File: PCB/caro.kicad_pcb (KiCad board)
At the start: 2 copper layers, 83.8 x 33 mm, 10 parts, among them SW1 Power Switch, SW2 Control Button, U1 DFR0299

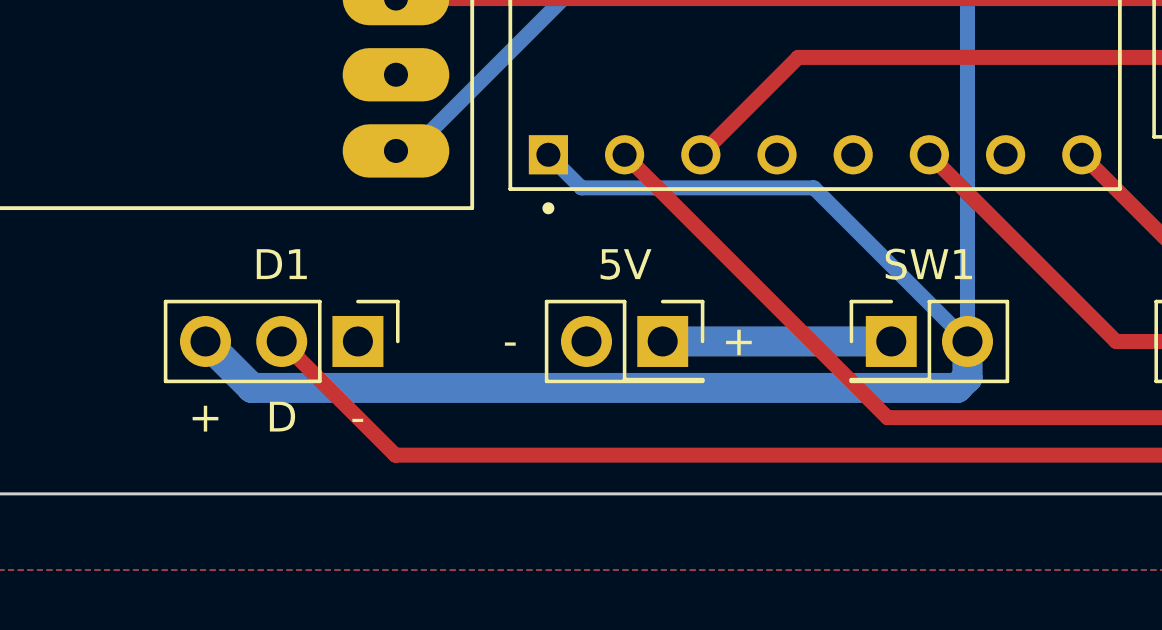
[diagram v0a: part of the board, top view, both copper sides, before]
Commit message: Corrected inverted LED pins
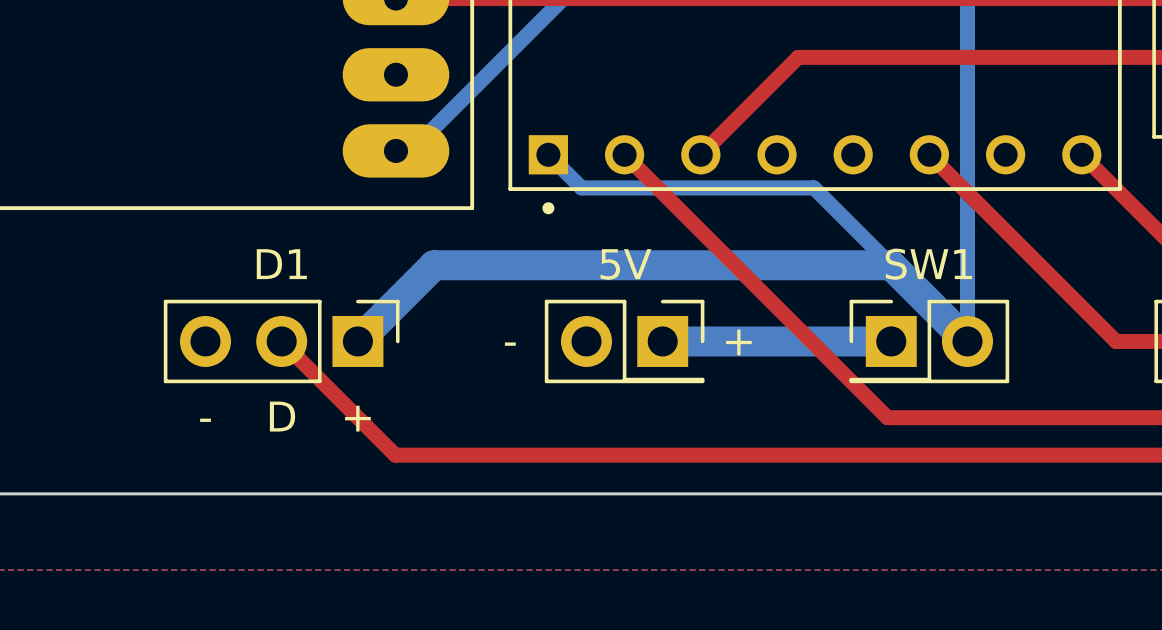
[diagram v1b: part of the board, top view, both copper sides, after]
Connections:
- D1 pad 1: GND -> 5V
- D1 pad 2: Net-(D1-Pad4) -> unconnected-(D1-Pad2)
- D1 pad 3: 5V -> GND
- R1 pad 1: Net-(D1-Pad4) -> D6
- R1 pad 2: D6 -> Net-(D1-Pad4)
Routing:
- net unconnected-(D1-Pad2): track 0.00 -> 60.0 mm
- net Net-(D1-Pad4): track 60.0 -> 20.1 mm
- net D6: track 20.1 -> 0.00 mm
- net 5V: track 71.6 -> 63.0 mm
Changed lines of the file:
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@@
   (net 46 "unconnected-(U1-Pad9)")
   (net 47 "+5V")
+  (net 48 "unconnected-(D1-Pad2)")
   (footprint "Module:Arduino_Nano" placed (layer "F.Cu")
     (at 147.32 101 90)
@@
     (fp_line (start -1.27 -0.635) (end -0.635 -1.27) (layer "F.Fab") (width 0.1))
     (pad "1" thru_hole rect locked (at 0 0 270) (size 1.7 1.7) (drill 1) (layers *.Cu *.Mask)
-      (net 7 "GND") (pinfunction "VDD") (pintype "power_in"))
+      (net 27 "5V") (pinfunction "VDD") (pintype "power_in"))
     (pad "2" thru_hole oval locked (at 0 2.54 270) (size 1.7 1.7) (drill 1) (layers *.Cu *.Mask)
-      (net 30 "Net-(D1-Pad4)") (pinfunction "DOUT") (pintype "output"))
+      (net 48 "unconnected-(D1-Pad2)") (pinfunction "DOUT") (pintype "output"))
     (pad "3" thru_hole oval locked (at 0 5.08 270) (size 1.7 1.7) (drill 1) (layers *.Cu *.Mask)
-      (net 27 "5V") (pinfunction "VSS") (pintype "power_in"))
+      (net 7 "GND") (pinfunction "VSS") (pintype "power_in"))
     (model "${KISYS3DMOD}/Connector_PinHeader_2.54mm.3dshapes/PinHeader_1x03_P2.54mm_Vertical.wrl"
       (offset (xyz 0 0 0))
@@
     (fp_line (start 14.66 1.6) (end 14.66 -1.6) (layer "F.Fab") (width 0.1))
     (pad "1" thru_hole circle locked (at 0 0) (size 1.6 1.6) (drill 0.8) (layers *.Cu *.Mask)
+      (net 17 "D6") (pintype "passive"))
+    (pad "2" thru_hole oval locked (at 20.32 0) (size 1.6 1.6) (drill 0.8) (layers *.Cu *.Mask)
       (net 30 "Net-(D1-Pad4)") (pintype "passive"))
-    (pad "2" thru_hole oval locked (at 20.32 0) (size 1.6 1.6) (drill 0.8) (layers *.Cu *.Mask)
-      (net 17 "D6") (pintype "passive"))
     (model "${KISYS3DMOD}/Resistor_THT.3dshapes/R_Axial_DIN0309_L9.0mm_D3.2mm_P20.32mm_Horizontal.wrl"
       (offset (xyz 0 0 0))
@@
     (effects (font (size 1 1) (thickness 0.15)))
   )
-  (gr_text "+" (at 111.76 111.76) (layer "F.SilkS")
+  (gr_text "+" (at 116.84 111.76) (layer "F.SilkS")
     (effects (font (size 1 1) (thickness 0.15)))
   )
@@
     (effects (font (size 1 1) (thickness 0.15)))
   )
-  (gr_text "-" (at 116.84 111.76) (layer "F.SilkS")
+  (gr_text "-" (at 111.76 111.76) (layer "F.SilkS")
     (effects (font (size 1 1) (thickness 0.15)))
   )
@@
   (segment (start 118.11 97.79) (end 150.53 97.79) (width 0.5) (layer "F.Cu") (net 16))
   (segment (start 150.53 97.79) (end 162.56 85.76) (width 0.5) (layer "F.Cu") (net 16))
-  (segment (start 173.32 106.68) (end 185.42 106.68) (width 0.5) (layer "F.Cu") (net 17))
-  (segment (start 167.64 101) (end 173.32 106.68) (width 0.5) (layer "F.Cu") (net 17))
   (segment (start 128.27 102.997) (end 131.516511 99.750489) (width 0.5) (layer "F.Cu") (net 19))
   (segment (start 131.516511 99.750489) (end 168.930489 99.750489) (width 0.5) (layer "F.Cu") (net 19))
   (segment (start 168.930489 99.750489) (end 170.18 101) (width 0.5) (layer "F.Cu") (net 19))
+  (segment (start 132.040511 104.100511) (end 134.62 106.68) (width 0.5) (layer "B.Cu") (net 27))
   (segment (start 124.293511 104.100511) (end 132.040511 104.100511) (width 0.5) (layer "B.Cu") (net 27))
-  (segment (start 136.81257 110.769511) (end 137.16 110.422081) (width 1) (layer "B.Cu") (net 27))
+  (segment (start 119.38 106.68) (end 134.62 106.68) (width 1) (layer "B.Cu") (net 27))
   (segment (start 123.19 102.997) (end 124.293511 104.100511) (width 0.5) (layer "B.Cu") (net 27))
-  (segment (start 132.040511 104.100511) (end 137.16 109.22) (width 0.5) (layer "B.Cu") (net 27))
-  (segment (start 111.76 109.22) (end 113.309511 110.769511) (width 1) (layer "B.Cu") (net 27))
   (segment (start 137.16 95.92) (end 147.32 85.76) (width 0.5) (layer "B.Cu") (net 27))
-  (segment (start 113.309511 110.769511) (end 136.81257 110.769511) (width 1) (layer "B.Cu") (net 27))
-  (segment (start 137.16 110.422081) (end 137.16 109.22) (width 1) (layer "B.Cu") (net 27))
+  (segment (start 116.84 109.22) (end 119.38 106.68) (width 1) (layer "B.Cu") (net 27))
+  (segment (start 134.62 106.68) (end 137.16 109.22) (width 1) (layer "B.Cu") (net 27))
   (segment (start 137.16 109.22) (end 137.16 95.92) (width 0.5) (layer "B.Cu") (net 27))
-  (segment (start 118.089511 113.009511) (end 165.617565 113.009511) (width 0.5) (layer "F.Cu") (net 30))
-  (segment (start 114.3 109.22) (end 118.089511 113.009511) (width 0.5) (layer "F.Cu") (net 30))
-  (segment (start 165.617565 113.009511) (end 166.349511 112.277565) (width 0.5) (layer "F.Cu") (net 30))
-  (segment (start 166.349511 112.277565) (end 166.349511 107.929511) (width 0.5) (layer "F.Cu") (net 30))
-  (segment (start 166.349511 107.929511) (end 165.1 106.68) (width 0.5) (layer "F.Cu") (net 30))
+  (segment (start 173.32 106.68) (end 185.42 106.68) (width 0.5) (layer "F.Cu") (net 30))
+  (segment (start 167.64 101) (end 173.32 106.68) (width 0.5) (layer "F.Cu") (net 30))
   (segment (start 134.493 111.76) (end 165.1 111.76) (width 0.5) (layer "F.Cu") (net 31))
   (segment (start 125.73 102.997) (end 134.493 111.76) (width 0.5) (layer "F.Cu") (net 31))
@@
   (segment (start 147.193 109.22) (end 147.32 109.22) (width 0.5) (layer "F.Cu") (net 45))
   (segment (start 127 109.22) (end 134.62 109.22) (width 1) (layer "B.Cu") (net 47))
+  (segment (start 118.089511 113.009511) (end 165.617565 113.009511) (width 0.5) (layer "F.Cu") (net 48))
+  (segment (start 114.3 109.22) (end 118.089511 113.009511) (width 0.5) (layer "F.Cu") (net 48))
+  (segment (start 165.617565 113.009511) (end 166.349511 112.277565) (width 0.5) (layer "F.Cu") (net 48))
+  (segment (start 166.349511 112.277565) (end 166.349511 107.929511) (width 0.5) (layer "F.Cu") (net 48))
+  (segment (start 166.349511 107.929511) (end 165.1 106.68) (width 0.5) (layer "F.Cu") (net 48))
   (zone (net 7) (net_name "GND") (layers F&B.Cu) (name "gnd") (hatch edge 0.508)
     (connect_pads (clearance 0.508))

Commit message: Bump to v1.1
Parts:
- moved R1 20.3 mm to (185.4, 106.7), turned to 180 degrees
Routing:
- net Net-(D1-Pad4): track 20.1 -> 0.00 mm
- net D6: track 0.00 -> 20.1 mm
- net 5V: track 63.0 -> 66.3 mm
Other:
- board text added: "Lightsaber v1.1 PCB Design by @simonmicro"
- board text removed: "Lightsaber v1.0 PCB Design by @simonmicro"
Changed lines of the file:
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@@
   )
   (footprint "Resistor_THT:R_Axial_DIN0309_L9.0mm_D3.2mm_P20.32mm_Horizontal" placed (layer "F.Cu")
-    (at 165.1 106.68)
+    (at 185.42 106.68 180)
     (descr "Resistor, Axial_DIN0309 series, Axial, Horizontal, pin pitch=20.32mm, 0.5W = 1/2W, length*diameter=9*3.2mm^2, http://cdn-reichelt.de/documents/datenblatt/B400/1_4W%23YAG.pdf")
     (tags "Resistor Axial_DIN0309 series Axial Horizontal pin pitch 20.32mm 0.5W = 1/2W length 9mm diameter 3.2mm")
@@
     (fp_line (start 5.66 -1.6) (end 5.66 1.6) (layer "F.Fab") (width 0.1))
     (fp_line (start 14.66 1.6) (end 14.66 -1.6) (layer "F.Fab") (width 0.1))
-    (pad "1" thru_hole circle locked (at 0 0) (size 1.6 1.6) (drill 0.8) (layers *.Cu *.Mask)
+    (pad "1" thru_hole circle locked (at 0 0 180) (size 1.6 1.6) (drill 0.8) (layers *.Cu *.Mask)
       (net 17 "D6") (pintype "passive"))
-    (pad "2" thru_hole oval locked (at 20.32 0) (size 1.6 1.6) (drill 0.8) (layers *.Cu *.Mask)
+    (pad "2" thru_hole oval locked (at 20.32 0 180) (size 1.6 1.6) (drill 0.8) (layers *.Cu *.Mask)
       (net 30 "Net-(D1-Pad4)") (pintype "passive"))
     (model "${KISYS3DMOD}/Resistor_THT.3dshapes/R_Axial_DIN0309_L9.0mm_D3.2mm_P20.32mm_Horizontal.wrl"
@@
     (effects (font (size 1 1) (thickness 0.15)))
   )
-  (gr_text "Lightsaber v1.0\nPCB Design by @simonmicro" (at 165.1 93.98) (layer "F.SilkS")
+  (gr_text "Lightsaber v1.1\nPCB Design by @simonmicro" (at 165.1 93.98) (layer "F.SilkS")
     (effects (font (size 1 1) (thickness 0.15)))
   )
@@
   (segment (start 118.11 97.79) (end 150.53 97.79) (width 0.5) (layer "F.Cu") (net 16))
   (segment (start 150.53 97.79) (end 162.56 85.76) (width 0.5) (layer "F.Cu") (net 16))
+  (segment (start 185.42 106.68) (end 173.32 106.68) (width 0.5) (layer "F.Cu") (net 17))
+  (segment (start 173.32 106.68) (end 167.64 101) (width 0.5) (layer "F.Cu") (net 17))
   (segment (start 128.27 102.997) (end 131.516511 99.750489) (width 0.5) (layer "F.Cu") (net 19))
   (segment (start 131.516511 99.750489) (end 168.930489 99.750489) (width 0.5) (layer "F.Cu") (net 19))
   (segment (start 168.930489 99.750489) (end 170.18 101) (width 0.5) (layer "F.Cu") (net 19))
-  (segment (start 132.040511 104.100511) (end 134.62 106.68) (width 0.5) (layer "B.Cu") (net 27))
   (segment (start 124.293511 104.100511) (end 132.040511 104.100511) (width 0.5) (layer "B.Cu") (net 27))
-  (segment (start 119.38 106.68) (end 134.62 106.68) (width 1) (layer "B.Cu") (net 27))
   (segment (start 123.19 102.997) (end 124.293511 104.100511) (width 0.5) (layer "B.Cu") (net 27))
+  (segment (start 137.16 106.68) (end 134.580511 104.100511) (width 0.5) (layer "B.Cu") (net 27))
+  (segment (start 137.16 109.22) (end 137.16 106.68) (width 0.5) (layer "B.Cu") (net 27))
   (segment (start 137.16 95.92) (end 147.32 85.76) (width 0.5) (layer "B.Cu") (net 27))
-  (segment (start 116.84 109.22) (end 119.38 106.68) (width 1) (layer "B.Cu") (net 27))
-  (segment (start 134.62 106.68) (end 137.16 109.22) (width 1) (layer "B.Cu") (net 27))
-  (segment (start 137.16 109.22) (end 137.16 95.92) (width 0.5) (layer "B.Cu") (net 27))
-  (segment (start 173.32 106.68) (end 185.42 106.68) (width 0.5) (layer "F.Cu") (net 30))
-  (segment (start 167.64 101) (end 173.32 106.68) (width 0.5) (layer "F.Cu") (net 30))
+  (segment (start 135.822081 111.76) (end 137.16 110.422081) (width 1) (layer "B.Cu") (net 27))
+  (segment (start 134.580511 104.100511) (end 132.040511 104.100511) (width 0.5) (layer "B.Cu") (net 27))
+  (segment (start 137.16 110.422081) (end 137.16 109.22) (width 1) (layer "B.Cu") (net 27))
+  (segment (start 137.16 106.68) (end 137.16 95.92) (width 0.5) (layer "B.Cu") (net 27))
+  (segment (start 119.38 111.76) (end 135.822081 111.76) (width 1) (layer "B.Cu") (net 27))
+  (segment (start 116.84 109.22) (end 119.38 111.76) (width 1) (layer "B.Cu") (net 27))
   (segment (start 134.493 111.76) (end 165.1 111.76) (width 0.5) (layer "F.Cu") (net 31))
   (segment (start 125.73 102.997) (end 134.493 111.76) (width 0.5) (layer "F.Cu") (net 31))
@@
   (segment (start 147.193 109.22) (end 147.32 109.22) (width 0.5) (layer "F.Cu") (net 45))
   (segment (start 127 109.22) (end 134.62 109.22) (width 1) (layer "B.Cu") (net 47))
-  (segment (start 118.089511 113.009511) (end 165.617565 113.009511) (width 0.5) (layer "F.Cu") (net 48))
-  (segment (start 114.3 109.22) (end 118.089511 113.009511) (width 0.5) (layer "F.Cu") (net 48))
+  (segment (start 164.216462 112.643538) (end 164.582435 113.009511) (width 0.5) (layer "F.Cu") (net 48))
+  (segment (start 166.349511 112.277565) (end 166.349511 107.929511) (width 0.5) (layer "F.Cu") (net 48))
   (segment (start 165.617565 113.009511) (end 166.349511 112.277565) (width 0.5) (layer "F.Cu") (net 48))
-  (segment (start 166.349511 112.277565) (end 166.349511 107.929511) (width 0.5) (layer "F.Cu") (net 48))
   (segment (start 166.349511 107.929511) (end 165.1 106.68) (width 0.5) (layer "F.Cu") (net 48))
+  (segment (start 117.723538 112.643538) (end 164.216462 112.643538) (width 0.5) (layer "F.Cu") (net 48))
+  (segment (start 114.3 109.22) (end 117.723538 112.643538) (width 0.5) (layer "F.Cu") (net 48))
+  (segment (start 164.582435 113.009511) (end 165.617565 113.009511) (width 0.5) (layer "F.Cu") (net 48))
   (zone (net 7) (net_name "GND") (layers F&B.Cu) (name "gnd") (hatch edge 0.508)
     (connect_pads (clearance 0.508))

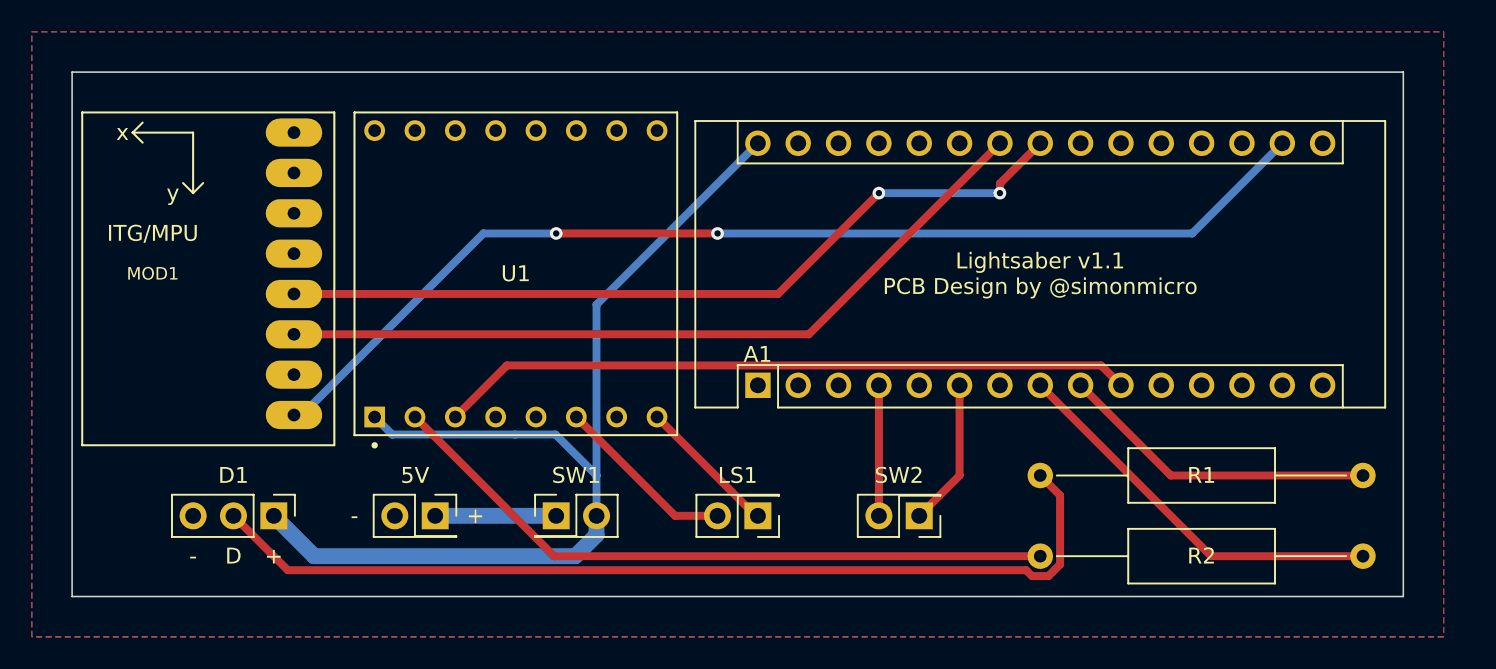
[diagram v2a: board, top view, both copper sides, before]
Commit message: Updated annotations Added missing control LED Reduced resistor sizes
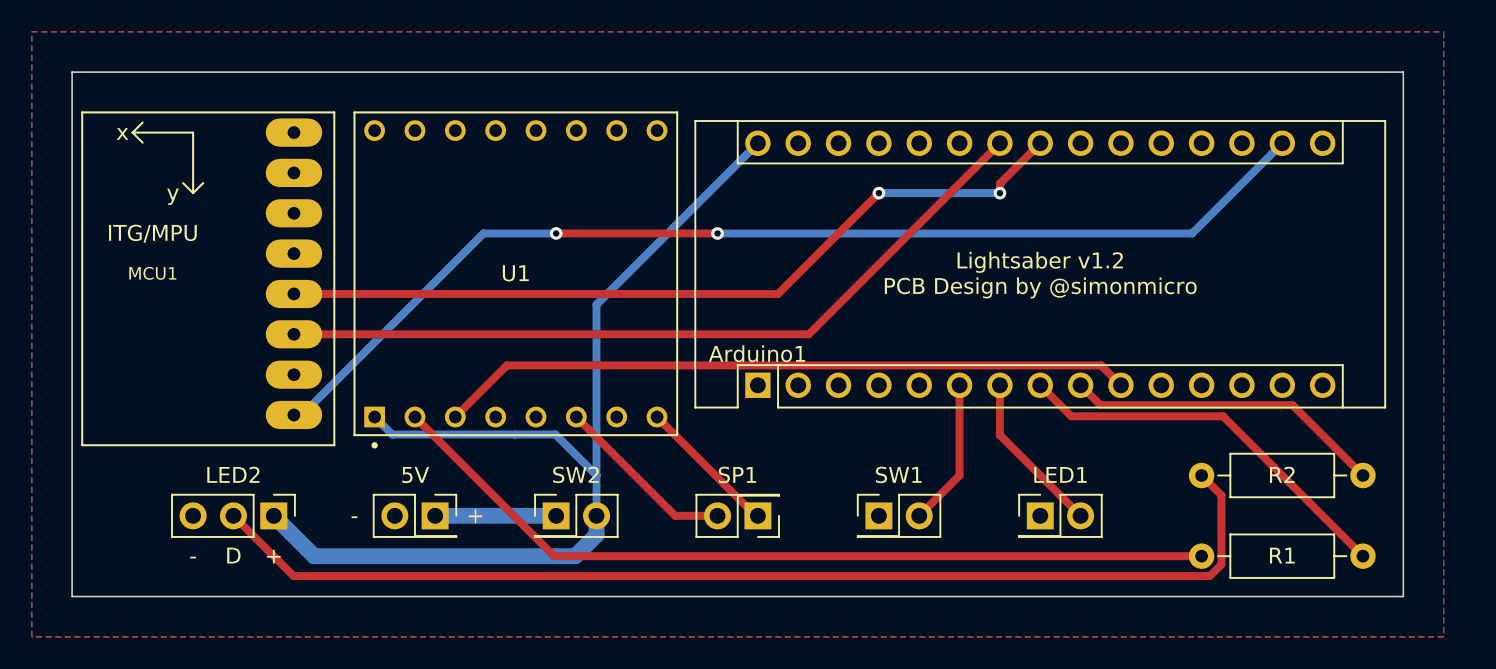
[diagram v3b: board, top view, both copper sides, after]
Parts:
- added LED1: Control Button LED, Connector_PinHeader_2.54mm:PinHeader_2x01_P2.54mm_Vertical, F.Cu at (165.1, 109.2)
- R1: renamed from R2; footprint Resistor_THT:R_Axial_DIN0309_L9.0mm_D3.2mm_P20.32mm_Horizontal -> Resistor_THT:R_Axial_DIN0207_L6.3mm_D2.5mm_P10.16mm_Horizontal
- R2: renamed from R1; footprint Resistor_THT:R_Axial_DIN0309_L9.0mm_D3.2mm_P20.32mm_Horizontal -> Resistor_THT:R_Axial_DIN0207_L6.3mm_D2.5mm_P10.16mm_Horizontal
- moved SW1 2.54 mm to (154.9, 109.2), turned to 0 degrees
- renumbered A1 to Arduino1, D1 to LED2, MOD1 to MCU1, LS1 to SP1, SW2 to SW1, SW1 to SW2
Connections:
- Arduino1 pad 7: unconnected-(A1-Pad7) -> D4
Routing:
- net Net-(LED2-Pad4): track 0.00 -> 70.2 mm
- net unconnected-(LED2-Pad2): track 60.0 -> 0.00 mm
- net D4: track 0.00 -> 10.3 mm
- net Net-(U1-Pad2): track 43.0 -> 53.2 mm
- net D3: track 9.27 -> 0.00 mm
- net GND: track 8.22 -> 9.27 mm
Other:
- board text added: "Lightsaber v1.2 PCB Design by @simonmicro"
- board text removed: "Lightsaber v1.1 PCB Design by @simonmicro"

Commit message: Revision v1.3 Increased HIGH_PWR width to 2mm
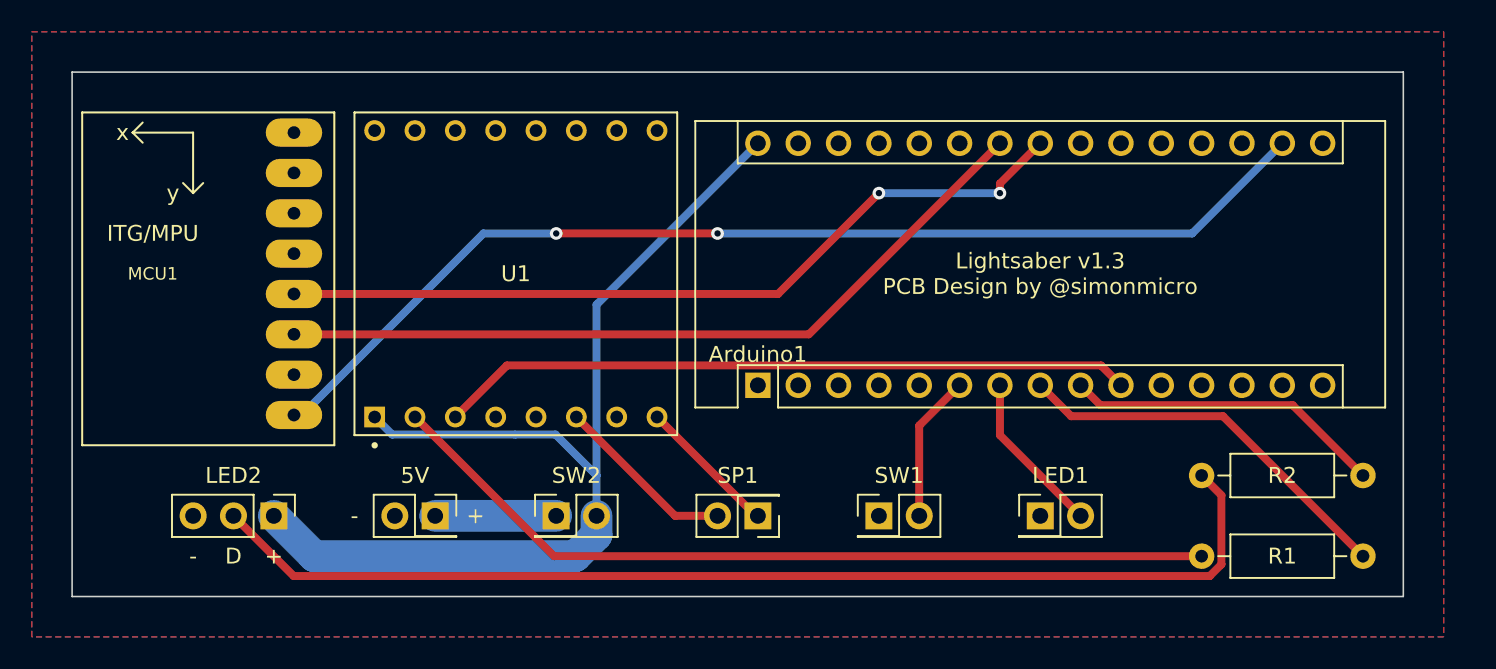
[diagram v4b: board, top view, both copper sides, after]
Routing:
- net GND: track 9.27 -> 0.00 mm
- net D3: track 0.00 -> 9.27 mm
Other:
- board text added: "Lightsaber v1.3 PCB Design by @simonmicro"
- board text removed: "Lightsaber v1.2 PCB Design by @simonmicro"
